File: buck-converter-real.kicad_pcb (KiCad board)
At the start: 4 copper layers, 64 x 64 mm, 110 parts, among them J1 Conn_01x02_Pin, J1 USB_C_Receptacle_USB2.0_16P, J10 I2C1, J11 SWD, J12 Conn_01x04, J13 CAN, J14 Conn_01x04, J15 Conn_01x06, J2 Conn_01x10, J3 MSD-1-A, J7 Conn_01x06, J8 I2C1, J9 SWD, Q1 CSD18540Q5B - 60-V, U1 AP2112K-3.3 (3V3 LDO), U10 TLV75733PDRV, U12 INA180A1, U2 CH32V203K8T6, U4 ZXTR2012K-13 12V@50mA vin<100V, U5 LM5109BMA, U6 TPT482-VS2R, U7 TCAN3414DDFR, U8 TPS61022, Y1 8MHz 20pF

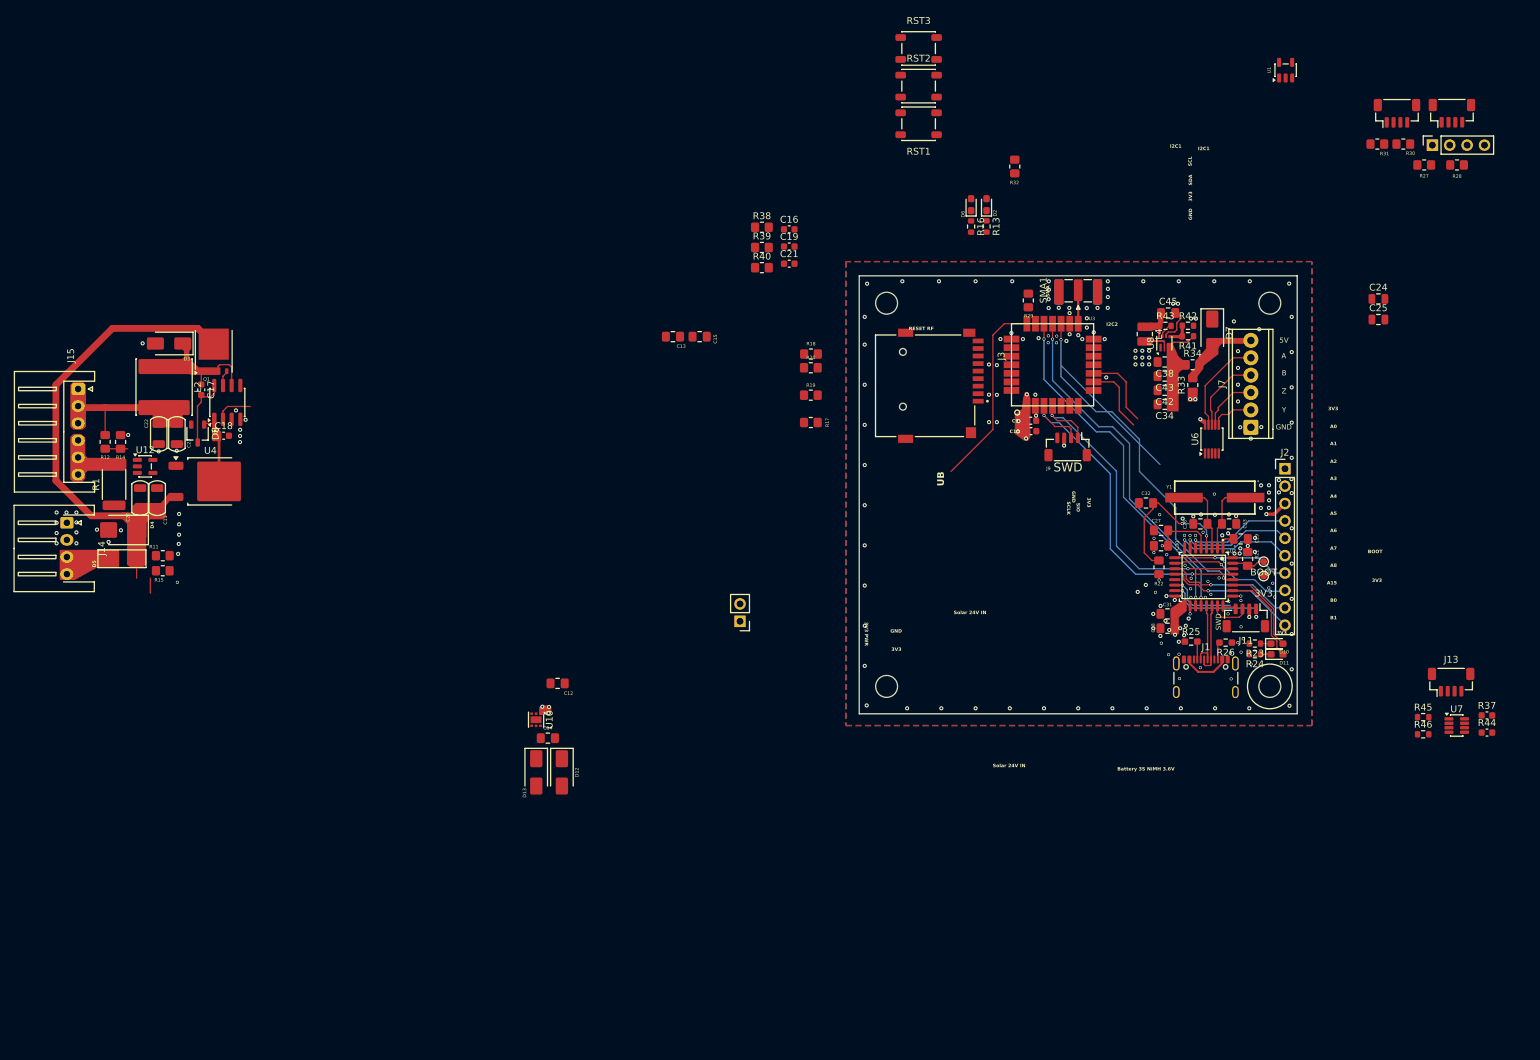
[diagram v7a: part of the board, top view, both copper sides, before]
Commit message: Swap to ideal diode
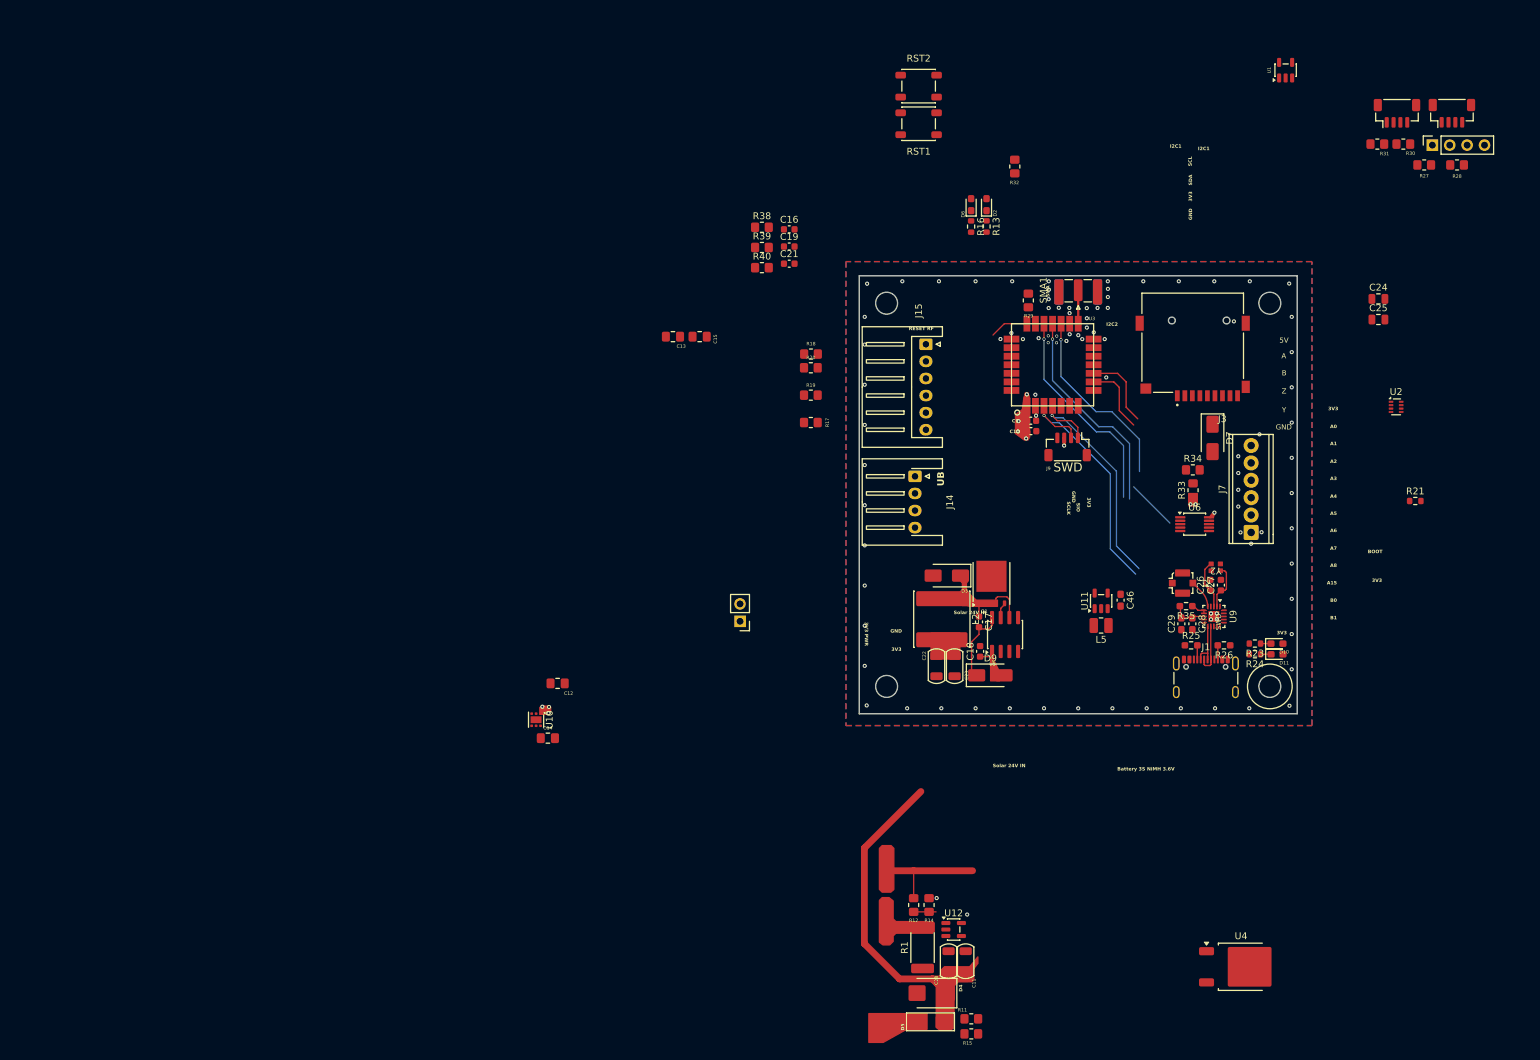
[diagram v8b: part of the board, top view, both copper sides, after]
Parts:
- removed C30: 1uF 25V, Capacitor_SMD:C_0805_2012Metric_Pad1.18x1.45mm_HandSolder
- removed C31: 10uF, Capacitor_SMD:C_0805_2012Metric_Pad1.18x1.45mm_HandSolder
- removed C32: 100nF 50V, Capacitor_SMD:C_0805_2012Metric_Pad1.18x1.45mm_HandSolder
- removed C33: 15pF C0G 50V, Capacitor_SMD:C_0805_2012Metric_Pad1.18x1.45mm_HandSolder
- removed C34: 100nF, Capacitor_SMD:C_0805_2012Metric_Pad1.18x1.45mm_HandSolder
- removed C38, C42, C43: 22uF 10V X7R/X5R 0805, Capacitor_SMD:C_0805_2012Metric_Pad1.18x1.45mm_HandSolder
- removed C45: 10uF 10V X7R/X5R 0805, Capacitor_SMD:C_0805_2012Metric_Pad1.18x1.45mm_HandSolder
- removed D12, D13: SS34 40V 3A, Diode_SMD:D_SMA
- removed D8: BAT54C, Package_TO_SOT_SMD:TSOT-23
- removed J11: SWD, Connector_JST:JST_SH_BM04B-SRSS-TB_1x04-1MP_P1.00mm_Vertical
- removed J13: CAN, Connector_JST:JST_SH_BM04B-SRSS-TB_1x04-1MP_P1.00mm_Vertical
- removed L4: 1uH lsat@5A 30mOhm AOTA-N252010S-1R0MT, Inductor_SMD:L_1008_2520Metric
- removed R22: 10K, Resistor_SMD:R_0805_2012Metric_Pad1.20x1.40mm_HandSolder
- removed R37, R44: 120, Capacitor_SMD:C_0603_1608Metric
- removed R41: 732k, Resistor_SMD:R_0603_1608Metric
- removed R42: 100k, Resistor_SMD:R_0603_1608Metric
- removed R43, R45, R46: 0, Resistor_SMD:R_0603_1608Metric
- removed RST3: SW_Omron_B3FS, Button_Switch_SMD:SW_SPST_PTS647_Sx38
- removed TP1: BOOT, TestPoint:TestPoint_Pad_D1.0mm
- removed TP2: 3V3, TestPoint:TestPoint_Pad_D1.0mm
- removed U7: TCAN3414DDFR, Package_TO_SOT_SMD:TSOT-23-8
- removed U8: TPS61022, Package_DFN_QFN:Texas_RWU0007A_VQFN-7_2x2mm_P0.5mm
- removed Y1: 8MHz 20pF, forest-ch:CRYSTAL-SMD_L11.4-W4.8-LS12.7
- added C46: 22uF 10V X7R/X5R 0603, Capacitor_SMD:C_0603_1608Metric_Pad1.08x0.95mm_HandSolder, F.Cu at (106.2, 115.4)
- added D9: SS510 100V, Diode_SMD:D_SMA, F.Cu at (87.2, 126.4)
- added L5: 4.7 uH, Inductor_SMD:L_1008_2520Metric, F.Cu at (103.3, 119.1)
- added R35: 1.5K, Resistor_SMD:R_0603_1608Metric_Pad0.98x0.95mm_HandSolder, F.Cu at (115.8, 116.3)
- added U11: TPS613222ADBV, Package_TO_SOT_SMD:SOT-23-5, F.Cu at (103.3, 115.5)
- added U9: ~, Package_DFN_QFN:QFN-20-1EP_3x3mm_P0.45mm_EP1.6x1.6mm, F.Cu at (119.8, 117.8)
- added Y2: Crystal_GND2, buck-forest:XRCGB32M000F1S1DR0, F.Cu at (120.1, 110.6)
- C26: value 15pF C0G 50V -> 18p; footprint Capacitor_SMD:C_0805_2012Metric_Pad1.18x1.45mm_HandSolder -> Capacitor_SMD:C_0603_1608Metric
- C27: value 100n 50V -> 18p; footprint Capacitor_SMD:C_0805_2012Metric_Pad1.18x1.45mm_HandSolder -> Capacitor_SMD:C_0603_1608Metric
- C28: value 100nF 50V -> 2.2u; footprint Capacitor_SMD:C_0805_2012Metric_Pad1.18x1.45mm_HandSolder -> Capacitor_SMD:C_0603_1608Metric_Pad1.08x0.95mm_HandSolder
- C29: value 100nF 50V -> 100n; footprint Capacitor_SMD:C_0805_2012Metric_Pad1.18x1.45mm_HandSolder -> Capacitor_SMD:C_0603_1608Metric_Pad1.08x0.95mm_HandSolder
- J2: value Conn_01x10 -> Conn_Coaxial; footprint Connector_PinHeader_2.54mm:PinHeader_1x10_P2.54mm_Vertical -> Connector_Coaxial:U.FL_Molex_MCRF_73412-0110_Vertical
- R21: value 10K -> 1m; footprint Resistor_SMD:R_0805_2012Metric_Pad1.20x1.40mm_HandSolder -> Resistor_SMD:R_0603_1608Metric
- U2: value CH32V203K8T6 -> ~; footprint forest-ch:LQFP-32_L7.0-W7.0-P0.80-LS9.0-BL -> Package_TO_SOT_SMD:SOT-583-8
- moved U4 166.5 mm to (123.8, 169.0)
- moved D5 136.2 mm to (78.4, 177.0)
- moved R15 136.2 mm to (84.4, 178.8)
- moved U12 136.2 mm to (81.8, 163.5)
- moved C11 136.2 mm to (83.6, 168.2)
- moved C20 136.2 mm to (81.1, 168.2)
- moved D4 136.2 mm to (78.6, 172.8)
- moved R1 136.2 mm to (77.3, 166.2)
- moved R11 136.2 mm to (84.4, 176.6)
- moved R12 136.2 mm to (76.0, 159.9)
- moved R14 136.2 mm to (78.2, 159.9)
- moved J14 124.1 mm to (76.2, 97.3)
- moved J15 124.1 mm to (77.7, 78.0)
- moved C17 118.6 mm to (85.5, 118.6)
- moved C22 118.6 mm to (79.3, 125.0)
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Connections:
- C22 pad 1: +BATT -> Net-(C22-Pad1)
- C23 pad 1: +BATT -> Net-(C22-Pad1)
- C26 pad 1: Net-(U2-OSC_OUT/PD1) -> Net-(U9-XI)
- C27 pad 1: +3.3V -> Net-(U9-XO)
- C28 pad 1: +3.3V -> Net-(U9-V5)
- C29 pad 1: +3.3V -> GND
- C29 pad 2: GND -> Net-(U9-V5)
- D10 pad 2: Net-(D10-A) -> unconnected-(D10-A-Pad2)
- D11 pad 2: Net-(D11-A) -> unconnected-(D11-A-Pad2)
- D2 pad 2: unconnected-(D2-A-Pad2) -> Net-(D2-A)
- J1 pad A6: Net-(U2-PA12/USB1DP) -> Net-(U9-PA1(D+))
- J1 pad A7: Net-(U2-PA11/USB1DM) -> Net-(U9-PA0(D-))
- J1 pad B6: Net-(U2-PA12/USB1DP) -> Net-(U9-PA1(D+))
- J1 pad B7: Net-(U2-PA11/USB1DM) -> Net-(U9-PA0(D-))
- J2 pad 1: VBUS -> Net-(J2-In)
- L2 pad 2: +BATT -> Net-(C22-Pad1)
- R12 pad 1: +BATT -> Net-(C22-Pad1)
- R21 pad 1: Net-(U2-PB8/BOOT0) -> Net-(U2-ON)
- U2 pad 1: +3.3V -> GND
- U2 pad 2: Net-(U2-OSC_IN/PD0) -> /BATT-IN
- U2 pad 3: Net-(U2-OSC_OUT/PD1) -> VBUS
- U2 pad 4: Net-(U2-NRST) -> Net-(U2-ON)
- U2 pad 5: +3.3V -> GND
- U2 pad 6: Net-(J2-Pin_4) -> +BATT
- U2 pad 7: Net-(J2-Pin_5) -> /BATT-IN
- U2 pad 8: Net-(J2-Pin_6) -> Net-(D2-A)
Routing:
- net /WIO-RST: track 71.2 -> 35.2 mm, vias 2 -> 1
- net /PWM_HI: track 34.3 -> 6.30 mm
- net Net-(U2-NRST): track 22.2 -> 0.00 mm, vias 2 -> 0
- net +3.3V: track 28.1 -> 7.68 mm, vias 20 -> 11
- net /UART-WIO-TX: track 51.6 -> 31.3 mm, vias 2 -> 1
- net /UART-WIO-RX: track 51.4 -> 31.5 mm, vias 2 -> 1
- net Net-(J2-Pin_10): track 19.5 -> 0.00 mm, vias 1 -> 0
- net Net-(J2-Pin_9): track 18.9 -> 0.00 mm, vias 1 -> 0
- net /Solar In: track 59.6 -> 41.0 mm
- net Net-(J2-Pin_8): track 18.0 -> 0.00 mm, vias 1 -> 0
- net Net-(J2-Pin_6): track 17.7 -> 0.00 mm, vias 1 -> 0
- net +BATT: track 17.2 -> 0.00 mm
- net Net-(C22-Pad1): track 0.00 -> 17.2 mm
- net Net-(J2-Pin_7): track 17.0 -> 0.00 mm, vias 1 -> 0
- net Net-(J2-Pin_5): track 16.7 -> 0.00 mm, vias 1 -> 0
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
